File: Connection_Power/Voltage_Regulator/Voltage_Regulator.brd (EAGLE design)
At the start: 20 x 13 mm, 7 parts, among them IC2 TS1117

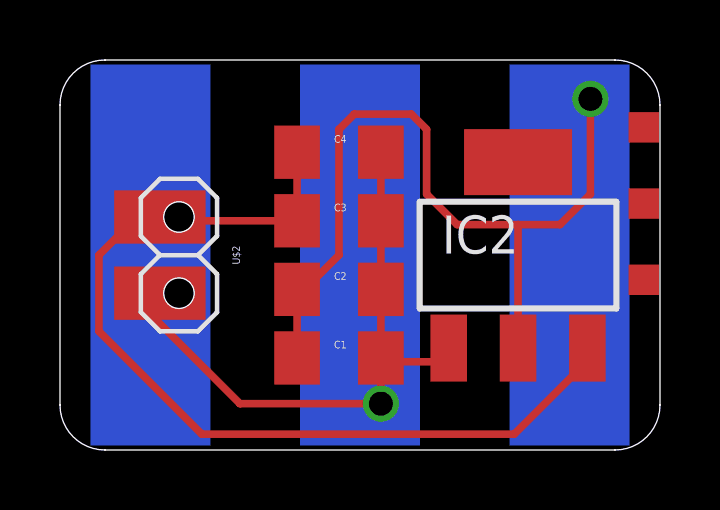
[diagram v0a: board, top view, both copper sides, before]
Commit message: Update Pinheader
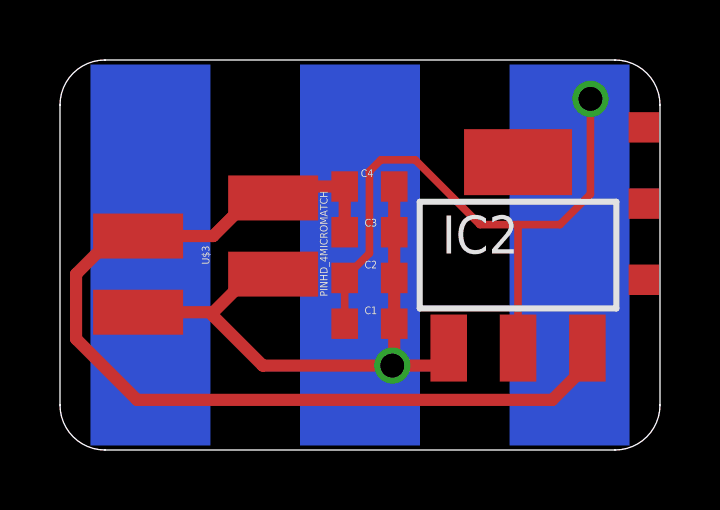
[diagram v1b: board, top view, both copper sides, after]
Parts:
- removed U$2: PINHD_22.54MOD, thar:PINHD_2_MOD
- added U$3: PINHD_4MICROMATCH, thar:MICROMATCH4P0L
- C1, C2, C3, C4: device thar:1206 -> thar:603
- moved C1 1.53 mm to (12.1, 5.46)
- moved C4 1.53 mm to (12.1, 10.0)
- moved C2 1.09 mm to (12.1, 6.99)
- moved C3 1.09 mm to (12.1, 8.51)
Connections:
- net GND: now also U$3.P$1, U$3.P$2; no longer U$2.P$2
- net N$2: now also U$3.P$3, U$3.P$4; no longer U$2.P$1
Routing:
- net VCC: track 32.8 -> 26.8 mm
- net N$2: track 32.8 -> 33.3 mm
